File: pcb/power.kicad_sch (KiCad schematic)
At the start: 39 parts, among them J1 12402012E212A, J2 S2B-PH-SM4-TB, SW1 EVQPUD02K, U1 TPD6S300ARUKR, U2 RT6160AWSC, U3 MAX20342EWG+, U4 BQ25150YFPT

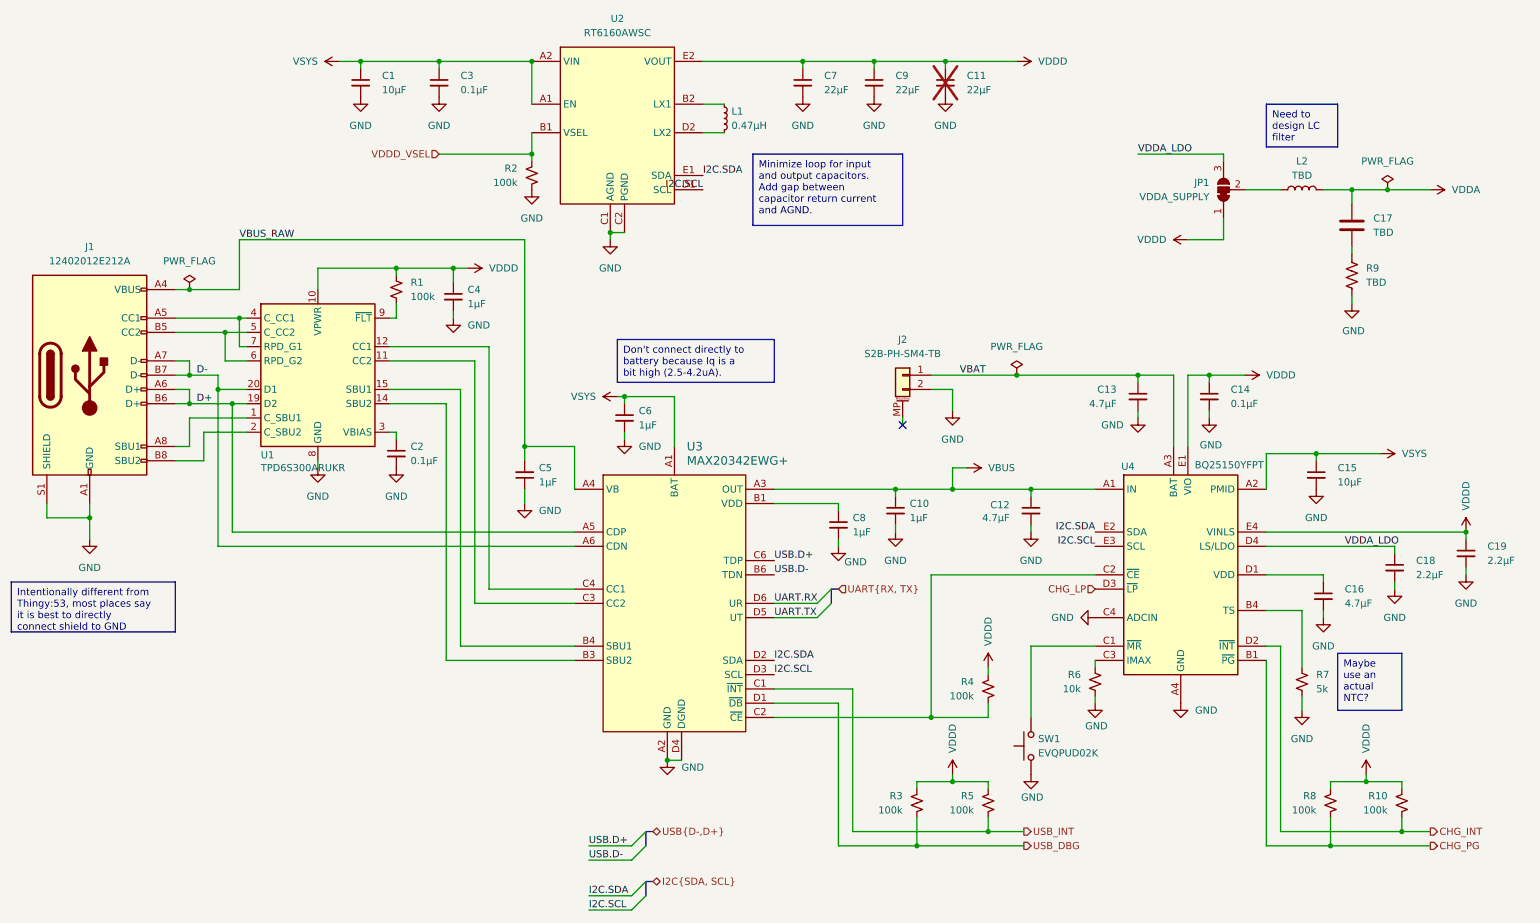
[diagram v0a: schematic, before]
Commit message: pcb: simplify power supply and define LC filter
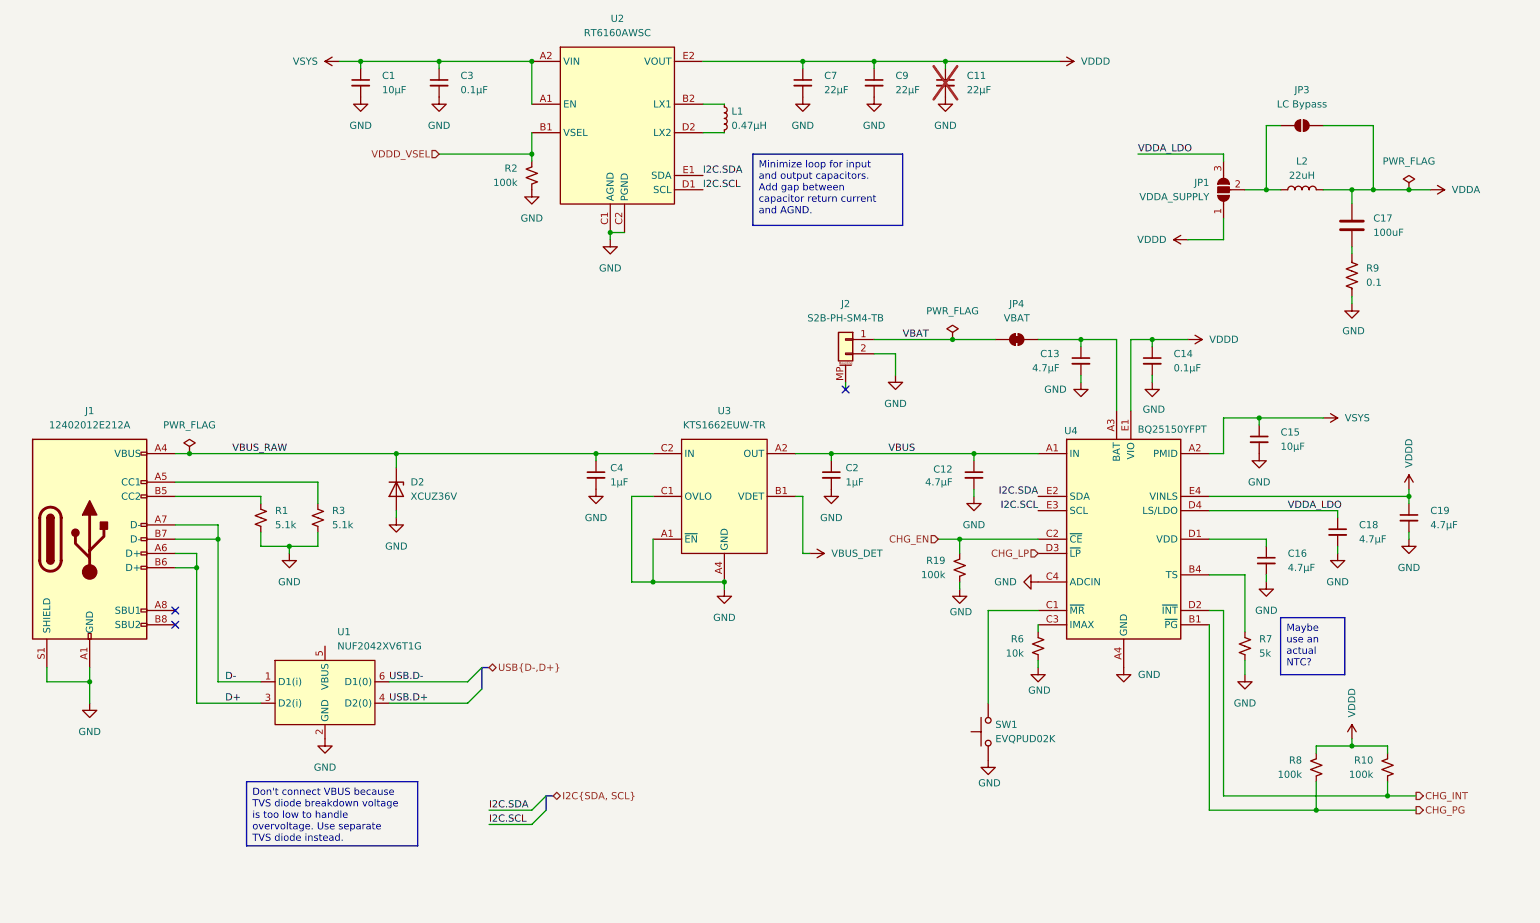
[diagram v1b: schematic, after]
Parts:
- removed C10, C6, C8: 1µF, Capacitor_SMD:C_0603_1608Metric, symbol Device:C_Small
- removed C5: 1µF, Capacitor_SMD:C_0805_2012Metric, symbol Device:C_Small
- removed R4, R5: 100k, Resistor_SMD:R_0402_1005Metric, symbol Device:R_Small_US
- removed U1: TPD6S300ARUKR, Package_DFN_QFN:WQFN-20-1EP_3x3mm_P0.4mm_EP1.7x1.7mm, symbol Power_Protection:TPD6S300A
- removed U3: MAX20342EWG+, zeus-le:Maxim_WLP-24_2.018x2.618mm_Layout6x4_P0.4mm_Ball0.27mm_Pad0.25mm_NSMD, symbol zeus-le:MAX20342EWG+
- added D2: XCUZ36V, Diode_SMD:D_SOD-323, symbol Diode:ZPYxx
- added JP3: LC Bypass, Jumper:SolderJumper-2_P1.3mm_Open_TrianglePad1.0x1.5mm, symbol Jumper:SolderJumper_2_Open
- added JP4: VBAT, Jumper:SolderJumper-2_P1.3mm_Bridged_RoundedPad1.0x1.5mm, symbol Jumper:SolderJumper_2_Bridged
- added R19: 100k, Resistor_SMD:R_0402_1005Metric, symbol Device:R_Small_US
- added U1: NUF2042XV6T1G, Package_TO_SOT_SMD:SOT-563, symbol zeus-le:NUF2042XV6
- added U3: KTS1662EUW-TR, zeus-le:Kinetic_WLCSP-12_1.94x1.28mm_Layout4x3_P0.4mm_Ball0.25mm_Pad0.25mm_NSMD, symbol zeus-le:KTS1662
- C17: value TBD -> 100uF; footprint Capacitor_SMD:C_0603_1608Metric -> Capacitor_SMD:C_1206_3216Metric; manf# (none) -> CL31A107MQHNNW
- C18, C19: value 2.2µF -> 4.7µF
- C2: value 0.1µF -> 1µF; footprint Capacitor_SMD:C_0402_1005Metric -> Capacitor_SMD:C_0603_1608Metric
- C4: manf# (none) -> CL10A105KB8NNNC, CL10B105KB8NQNC
- JP1: symbol Jumper:SolderJumper_3_Bridged12 -> Jumper:SolderJumper_3_Open
- L2: value TBD -> 22uH; footprint (none) -> Inductor_SMD:L_0805_2012Metric; manf# (none) -> MLZ2012N220LT000
- R1, R3: value 100k -> 5.1k
- R9: value TBD -> 0.1
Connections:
- net USB_DBG is gone; now on net GND: R3.2
- net D+: now also U1.3 (D2(i))
- net D-: now also U1.1 (D1(i))
- net GND: now also R1.2, D2.2 (A), R19.2, U1.2 (GND), U3.A1 (~{EN}), U3.A4 (GND), U3.B4 (GND), U3.C1 (OVLO), U3.C4 (GND)
- net USB.D+: now also U1.4 (D2(0))
- net USB.D-: now also U1.6 (D1(0))
- net VBAT: now also JP4.1 (A); no longer C13.1, U4.A3 (BAT), U4.B3 (BAT)
- net VBUS: now also C2.1, U3.A2 (OUT), U3.A3 (OUT), U3.B2 (OUT)
- net VBUS_RAW: now also C4.1, D2.1 (K), U3.B3 (IN), U3.C2 (IN), U3.C3 (IN)
- net VDDA: now also JP3.2 (B)
- net VDDD: no longer C4.1, R1.1, R3.1
- net CHG_EN: now reaches U4.C2 (~{CE})
- net CHG_EN: now also R19.1
- net at J1.A5 (CC1): now also R3.1
- net at J1.B5 (CC2): now also R1.1
- net at JP1.2 (C), L2.1: now also JP3.1 (A)
- new net: C13.1, JP4.2 (B), U4.A3 (BAT), U4.B3 (BAT)
- new net VBUS_DET: U3.B1 (VDET)
- no-connect marks 1 -> 3
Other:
- moved on the sheet: C12, C13, C14, C15, C16, C18, C19, J1, J2, R10, R6, R7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

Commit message: pcb: pretty much the final version
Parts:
- added J6: B2B-PH-K-S, Connector_JST:JST_PH_B2B-PH-K_1x02_P2.00mm_Vertical, symbol Connector_Generic:Conn_01x02
- C1, C15: manf# (none) -> GRM188R61A106ME69D
- C12, C13, C16, C18, C19: manf# (none) -> CL10A475MA8NQN
- C14, C3: manf# (none) -> CL05A104KA5NNNC
- C2: manf# (none) -> CL10B105KP8NNNC
- C4: manf# CL10A105KB8NNNC, CL10B105KB8NQNC -> CL10A105KB8NNNC
- D2: manf# (none) -> XCUZ36V
- J1: Manufacturer Amphenol -> (none); manf# (none) -> 12402012E212A
- J2: Manufacturer JST -> (none); manf# (none) -> S2B-PH-SM4-TB
- JP3: manf# (none) -> LC Bypass
- R1, R3: manf# (none) -> CR0402-JW-512GLF
- R10, R19, R2, R8: manf# (none) -> WR04X1003FTL
- R6: manf# (none) -> CR0402-JW-103GLF
- R7: manf# (none) -> RC0402FR-075KL
- R9: footprint Resistor_SMD:R_0402_1005Metric -> Resistor_SMD:R_0603_1608Metric; manf# (none) -> CRL0603-FW-R100ELF
- SW1: manf# EVQ-P7D01P -> EVQPUD02K
- U1: manf# (none) -> NUF2042XV6T1G
- U2: manf# (none) -> RT6160AWSC
- U3: manf# (none) -> KTS1662EUW-TR
- U4: value BQ25150YFPT -> BQ25150YFPR; footprint zeus-le:Texas_DSBGA-20_1.615x2.015mm_Layout4x5_P0.4mm -> zeus-le:Texas_DSBGA-20_1.615x2.015mm_Layout4x5_P0.4mm_NSMD; manf# (none) -> BQ25150YFPR
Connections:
- net GND: now also J6.2 (Pin_2)
- net VBAT: now also J6.1 (Pin_1)
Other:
- moved on the sheet: C13, J2, JP4

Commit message: pcb: rotate debug connector
This prevents it from interfering with the USB connector.
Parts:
- C12, C13, C16, C18, C19: manf# CL10A475MA8NQN -> C1608X5R1E475K080AC
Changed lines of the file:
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@@
 			)
 		)
-		(property "manf#" "CL10A475MA8NQN"
+		(property "manf#" "C1608X5R1E475K080AC"
 			(at 251.46 106.68 0)
 			(effects
@@
 			)
 		)
-		(property "manf#" "CL10A475MA8NQN"
+		(property "manf#" "C1608X5R1E475K080AC"
 			(at 205.74 78.74 0)
 			(effects
@@
 			)
 		)
-		(property "manf#" "CL10A475MA8NQN"
+		(property "manf#" "C1608X5R1E475K080AC"
 			(at 186.69 96.52 0)
 			(effects
@@
 			)
 		)
-		(property "manf#" "CL10A475MA8NQN"
+		(property "manf#" "C1608X5R1E475K080AC"
 			(at 238.76 111.76 0)
 			(effects
@@
 			)
 		)
-		(property "manf#" "CL10A475MA8NQN"
+		(property "manf#" "C1608X5R1E475K080AC"
 			(at 264.16 104.14 0)
 			(effects

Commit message: pcb: rev 1.0 version submitted for manufacturing
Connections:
- no-connect marks 3 -> 4
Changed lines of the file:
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@@
 	)
 	(junction
-		(at 186.69 74.93)
-		(diameter 0)
-		(color 0 0 0 0)
-	)
-	(junction
 		(at 254 45.72)
 		(diameter 0)
@@
 	)
 	(no_connect
+		(at 71.12 127)
+	)
+	(no_connect
 		(at 44.45 123.19)
 	)
@@
 	(wire
 		(pts
-			(xy 175.26 74.93) (xy 186.69 74.93)
+			(xy 175.26 74.93) (xy 191.77 74.93)
 		)
 		(stroke
@@
 	(wire
 		(pts
-			(xy 186.69 74.93) (xy 191.77 74.93)
-		)
-		(stroke
-			(width 0)
-			(type default)
-		)
-	)
-	(wire
-		(pts
 			(xy 199.39 74.93) (xy 205.74 74.93)
 		)
@@
 	)
 	(symbol
-		(lib_id "power:PWR_FLAG")
-		(at 186.69 74.93 0)
+		(lib_id "Device:C_Small")
+		(at 91.44 26.67 0)
 		(unit 1)
 		(exclude_from_sim no)
@@
 		(on_board yes)
 		(dnp no)
-		(fields_autoplaced yes)
-		(property "Reference" "#FLG02"
-			(at 186.69 73.025 0)
+		(property "Reference" "C3"
+			(at 95.25 25.3999 0)
 			(effects
 				(font
 					(size 1.27 1.27)
 				)
-				(hide yes)
+				(justify left)
 			)
 		)
-		(property "Value" "PWR_FLAG"
-			(at 186.69 69.85 0)
+		(property "Value" "0.1µF"
+			(at 95.25 27.9399 0)
 			(effects
 				(font
 					(size 1.27 1.27)
 				)
+				(justify left)
 			)
 		)
-		(property "Footprint" ""
-			(at 186.69 74.93 0)
+		(property "Footprint" "Capacitor_SMD:C_0402_1005Metric"
+			(at 91.44 26.67 0)
 			(effects
 				(font
@@
 		)
 		(property "Datasheet" "~"
-			(at 186.69 74.93 0)
+			(at 91.44 26.67 0)
 			(effects
 				(font
@@
 			)
 		)
-		(property "Description" "Special symbol for telling ERC where power comes from"
-			(at 186.69 74.93 0)
+		(property "Description" "Capacitor, decoupling, 25V, X5R"
+			(at 91.44 26.67 0)
+			(effects
+				(font
+					(size 1.27 1.27)
+				)
+				(hide yes)
+			)
+		)
+		(property "manf#" "CL05A104KA5NNNC"
+			(at 91.44 26.67 0)
 			(effects
 				(font
@@
 			)
 		)
+		(pin "2"
+		)
 		(pin "1"
 		)
@@
 			(project "zeus-le"
 				(path "/45d4abf7-8cf8-470c-bd26-f127279c8d1b/6cd3ad24-f296-403f-8ce8-fedfc8e5b734"
-					(reference "#FLG02")
+					(reference "C3")
 					(unit 1)
 				)
@@
 	)
 	(symbol
-		(lib_id "Device:C_Small")
-		(at 91.44 26.67 0)
+		(lib_id "power:PWR_FLAG")
+		(at 205.74 74.93 0)
 		(unit 1)
 		(exclude_from_sim no)
@@
 		(on_board yes)
 		(dnp no)
-		(property "Reference" "C3"
-			(at 95.25 25.3999 0)
+		(fields_autoplaced yes)
+		(property "Reference" "#FLG02"
+			(at 205.74 73.025 0)
 			(effects
 				(font
 					(size 1.27 1.27)
 				)
-				(justify left)
+				(hide yes)
 			)
 		)
-		(property "Value" "0.1µF"
-			(at 95.25 27.9399 0)
+		(property "Value" "PWR_FLAG"
+			(at 205.74 69.85 0)
 			(effects
 				(font
 					(size 1.27 1.27)
 				)
-				(justify left)
 			)
 		)
-		(property "Footprint" "Capacitor_SMD:C_0402_1005Metric"
-			(at 91.44 26.67 0)
+		(property "Footprint" ""
+			(at 205.74 74.93 0)
 			(effects
 				(font
@@
 		)
 		(property "Datasheet" "~"
-			(at 91.44 26.67 0)
-			(effects
-				(font
-					(size 1.27 1.27)
-				)
-				(hide yes)
-			)
-		)
-		(property "Description" "Capacitor, decoupling, 25V, X5R"
-			(at 91.44 26.67 0)
+			(at 205.74 74.93 0)
 			(effects
 				(font
@@
 			)
 		)
-		(property "manf#" "CL05A104KA5NNNC"
-			(at 91.44 26.67 0)
+		(property "Description" "Special symbol for telling ERC where power comes from"
+			(at 205.74 74.93 0)
 			(effects
 				(font
@@
 			)
 		)
-		(pin "2"
-		)
 		(pin "1"
 		)
@@
 			(project "zeus-le"
 				(path "/45d4abf7-8cf8-470c-bd26-f127279c8d1b/6cd3ad24-f296-403f-8ce8-fedfc8e5b734"
-					(reference "C3")
+					(reference "#FLG02")
 					(unit 1)
 				)

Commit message: pcb: replace inductor
Replace power supply inductor with a more readily available and cheaper
part.
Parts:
- L1: footprint Inductor_SMD:L_Coilcraft_XxL4020 -> zeus-le:L_Bourns_SRP4020FA_4.1x4.1mm; manf# XFL4015-471MEC -> SRP4020FA-R47M
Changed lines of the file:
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@@
 			)
 		)
-		(property "Footprint" "Inductor_SMD:L_Coilcraft_XxL4020"
+		(property "Footprint" "zeus-le:L_Bourns_SRP4020FA_4.1x4.1mm"
 			(at 142.24 33.02 0)
 			(effects
@@
 			)
 		)
-		(property "manf#" "XFL4015-471MEC"
+		(property "manf#" "SRP4020FA-R47M"
 			(at 142.24 33.02 0)
 			(effects

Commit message: pcb: add pull-downs for WiFi power
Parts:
- U3: value KTS1662EUW-TR -> KTS1662EUW-TR
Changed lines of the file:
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@@
 			)
 		)
-		(property "Value" " KTS1662EUW-TR"
+		(property "Value" "KTS1662EUW-TR"
 			(at 142.24 87.63 0)
 			(effects
